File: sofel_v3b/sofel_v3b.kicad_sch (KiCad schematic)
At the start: 81 parts, among them J1 Pimaroni Trackball, J2 4PIN, J3 OLED, J5 Conn_01x05_Socket, J6 Conn_01x05_Socket, Q1 TIP120, SW1 SW_PUSH_LED, SW10 SW_PUSH_LED, SW11 SW_PUSH_LED, SW12 SW_PUSH_LED, SW13 SW_PUSH_LED, SW14 SW_PUSH_LED, SW15 SW_PUSH_LED, SW16 SW_PUSH_LED, SW17 SW_PUSH_LED, SW18 SW_PUSH_LED, SW19 SW_PUSH_LED, SW2 SW_PUSH_LED, SW20 SW_PUSH_LED, SW21 SW_PUSH_LED, SW22 SW_PUSH_LED, SW23 SW_PUSH_LED, SW24 SW_PUSH_LED, SW25 Rotary_Encoder_Switch, SW26 SW_PUSH_LED, SW27 SW_PUSH_LED, SW28 SW_PUSH_LED, SW29 SW_PUSH_LED, SW3 SW_PUSH_LED, SW30 SW_PUSH_LED, SW4 SW_PUSH_LED, SW5 SW_PUSH_LED, SW6 SW_PUSH_LED, SW7 SW_PUSH_LED, SW8 SW_PUSH_LED, SW9 SW_PUSH_LED, U2 SN74AHCT1G125, U3 Pico

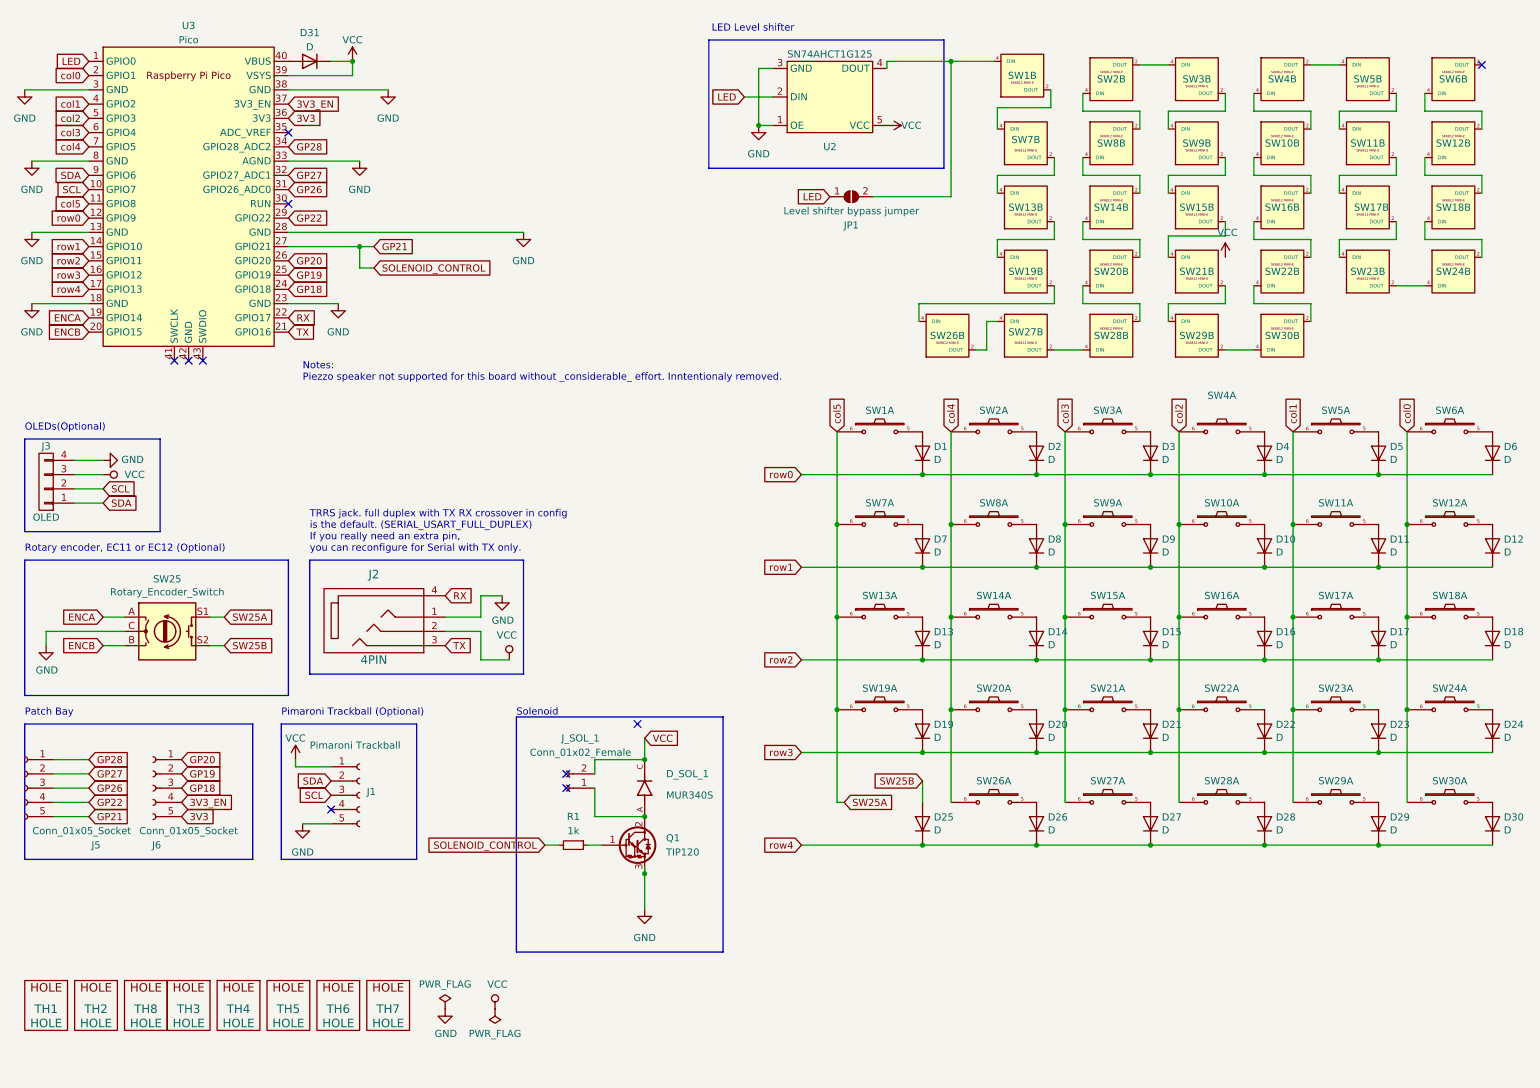
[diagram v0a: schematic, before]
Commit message: Removed solenoid from PCB left soleniod in schematic Updated schematic title block and size
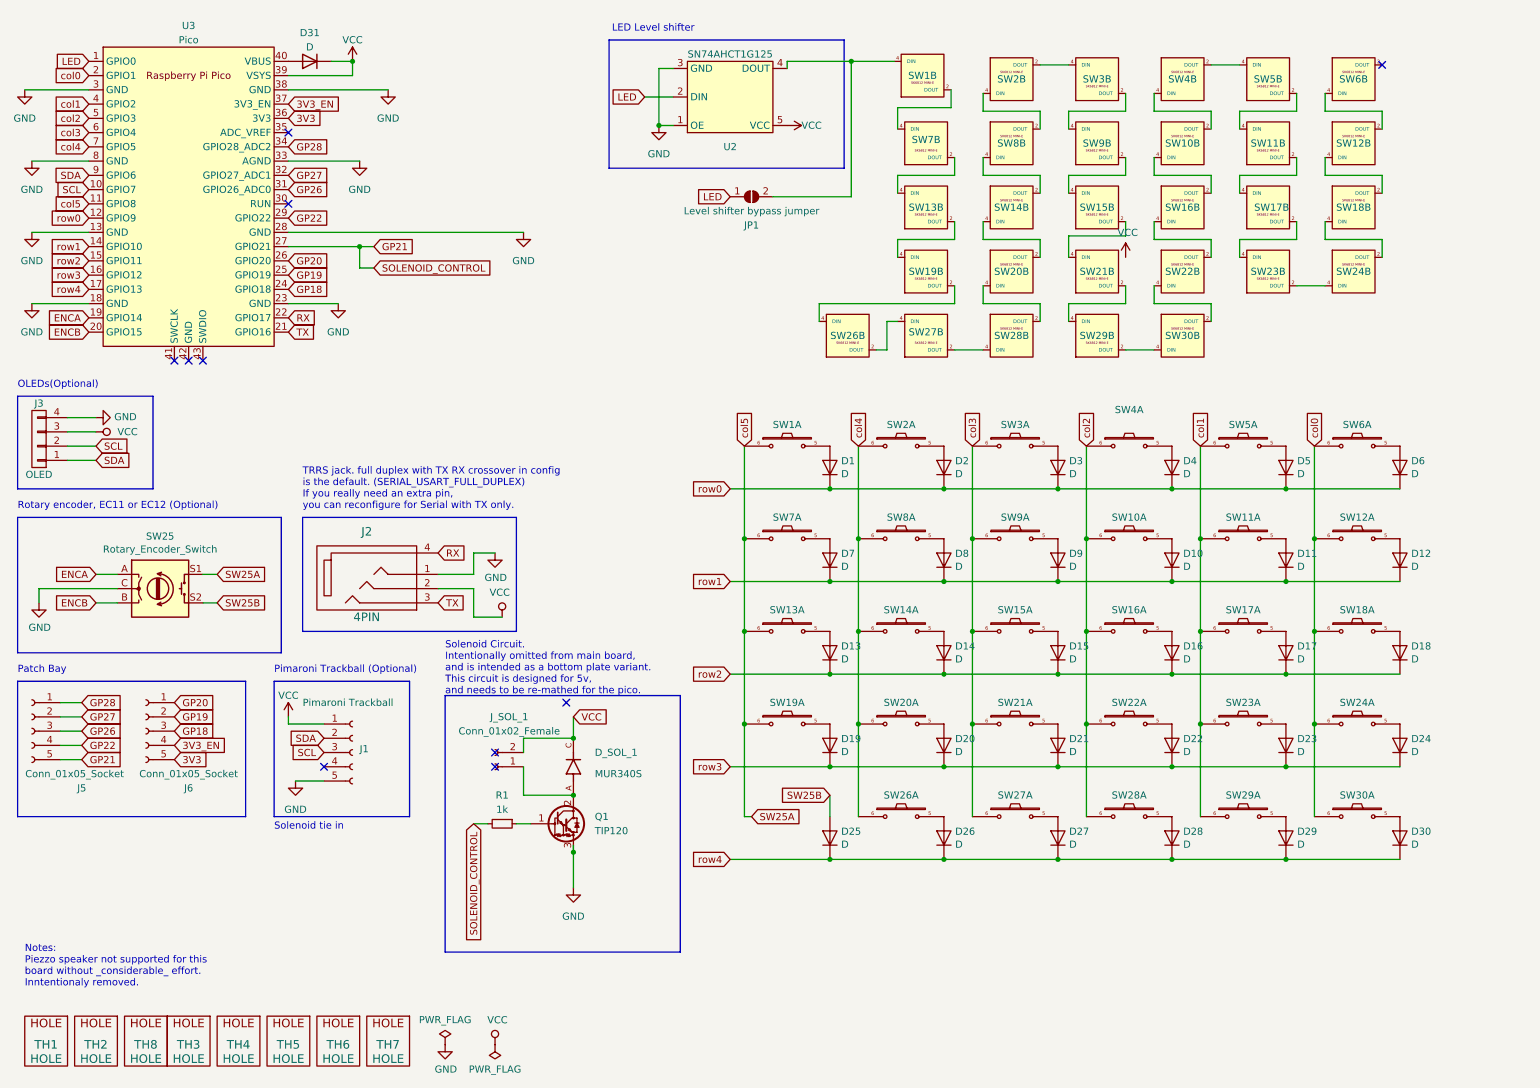
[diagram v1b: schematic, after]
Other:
- note added: "Solenoid Circuit. Intentionally omitted from main board, and is intended as a bottom plate variant. This circuit is designed for 5v, and needs to be re-mathed for the pico."
- note added: "Solenoid tie in"
- note removed: "Solenoid"
- title: (none) -> Sofle Pico
- moved on the sheet: D1, D10, D11, D12, D13, D14, D15, D16, D17, D18, D19, D2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

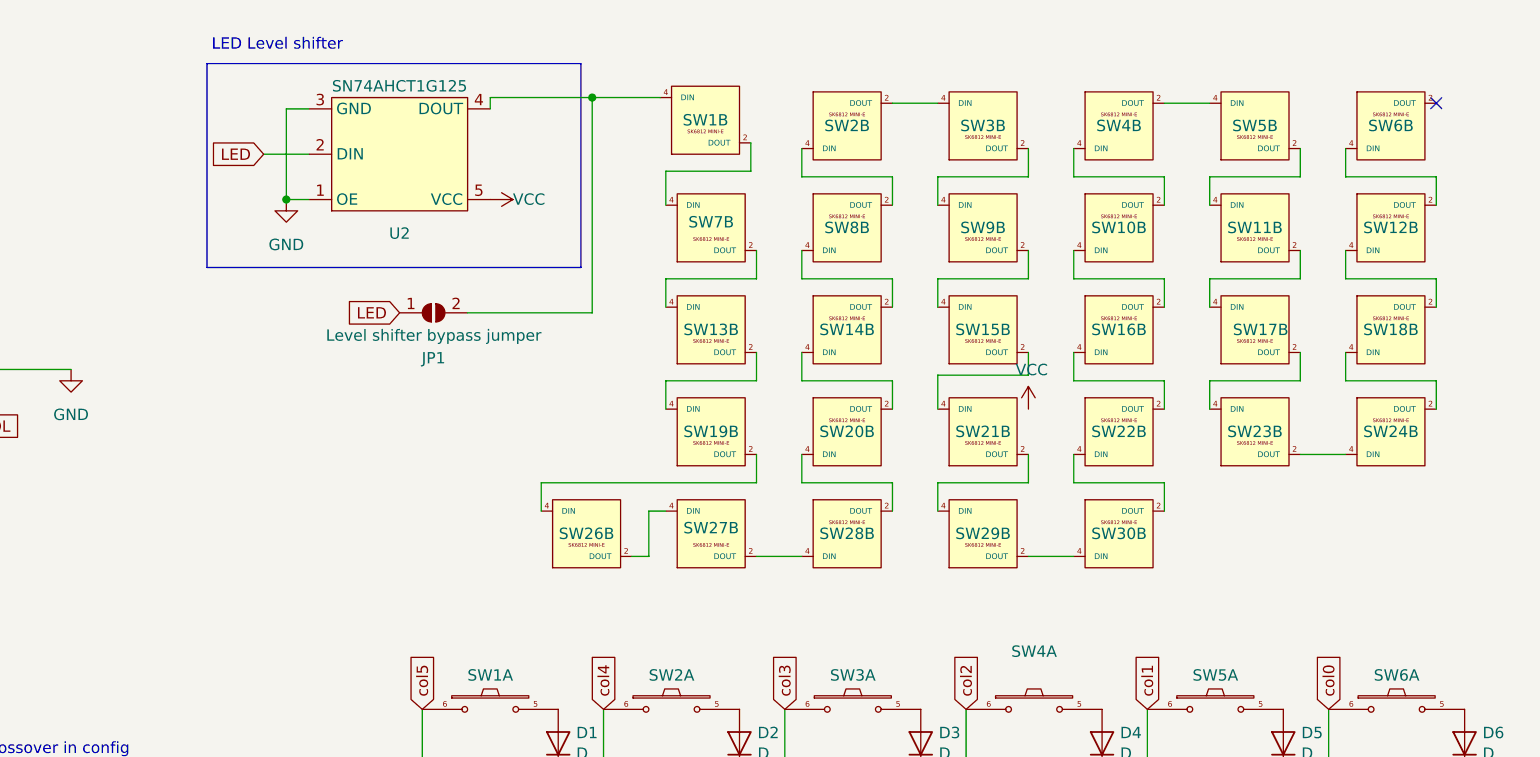
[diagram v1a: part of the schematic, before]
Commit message: Added double-sided level shifter
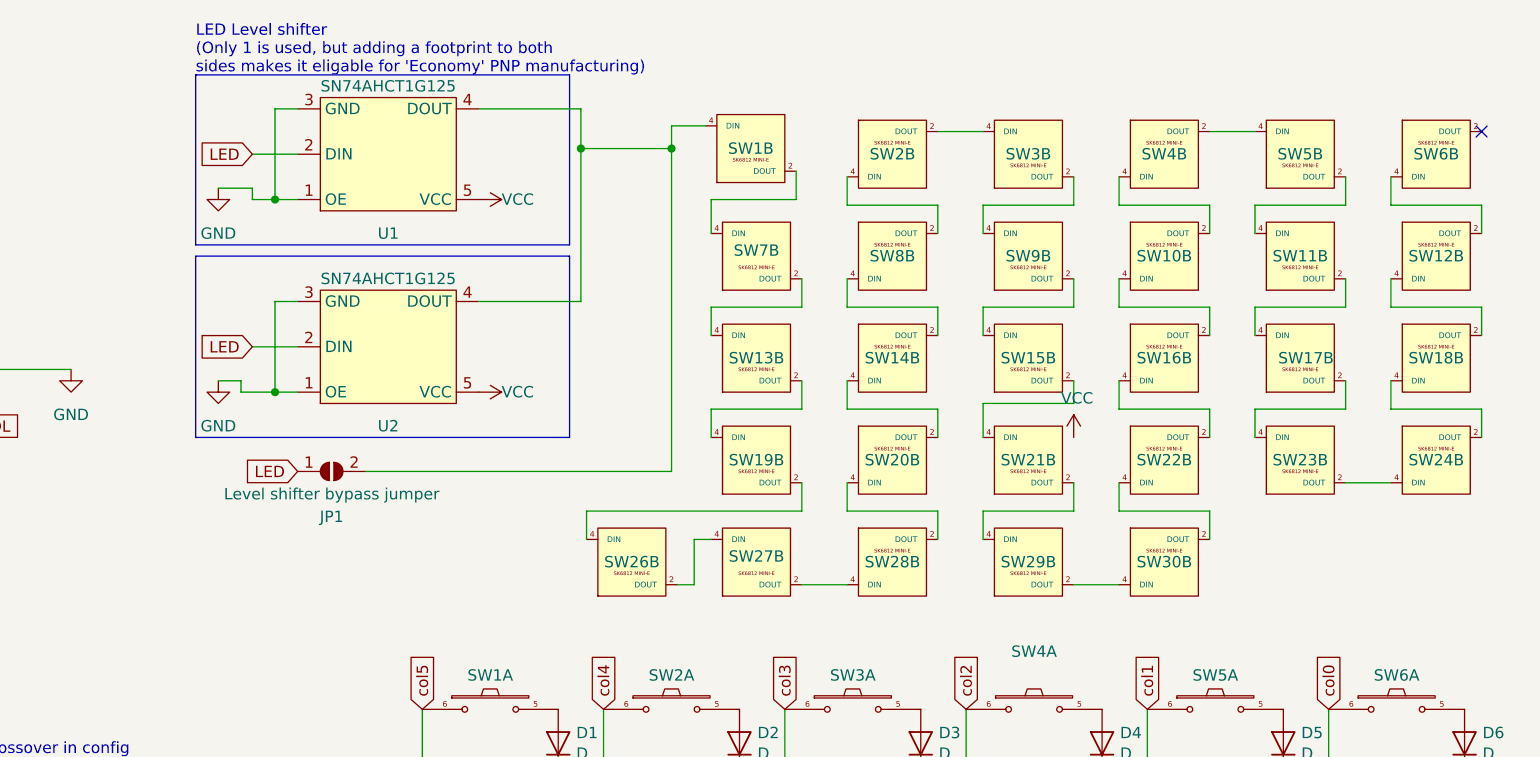
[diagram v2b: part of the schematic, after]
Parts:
- added U1: SN74AHCT1G125, sofle_v3b:SN74AHCT1G125 - Junco, symbol Junco:SN74AHCT1G125
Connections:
- net GND: now also U1.1 (OE), U1.3 (GND)
- net LED: now also U1.2 (DIN)
- net VCC: now also U1.5 (VCC)
- net at JP1.2 (B), SW1.4 (DIN), U2.4 (DOUT): now also U1.4 (DOUT)
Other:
- note added: "LED Level shifter (Only 1 is used, but adding a footprint to both sides makes it eligable for 'Economy' PNP manufacturing)"
- note removed: "LED Level shifter"
- moved on the sheet: JP1, SW10B, SW11B, SW12B, SW13B, SW14B, SW15B, SW16B, SW17B, SW18B, SW19B, SW1B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

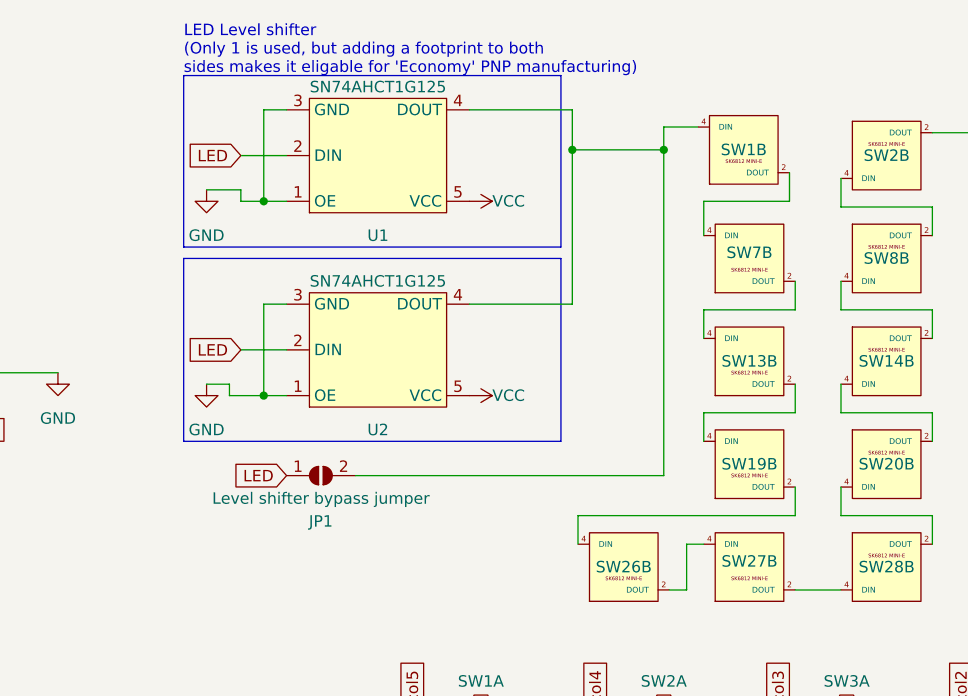
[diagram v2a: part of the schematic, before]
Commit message: Rolled back the double level shifter
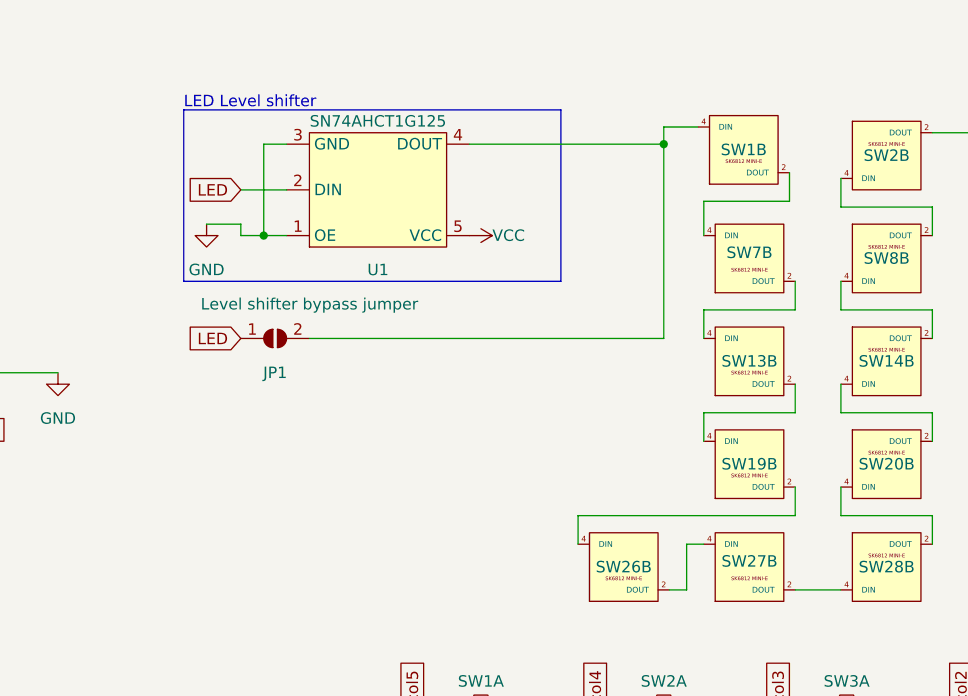
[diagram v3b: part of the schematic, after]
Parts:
- removed U2: SN74AHCT1G125, sofle_v3b:SN74AHCT1G125 - Junco, symbol Junco:SN74AHCT1G125
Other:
- note added: "LED Level shifter"
- note removed: "LED Level shifter (Only 1 is used, but adding a footprint to both sides makes it eligable for 'Economy' PNP manufacturing)"
- moved on the sheet: JP1, U1
